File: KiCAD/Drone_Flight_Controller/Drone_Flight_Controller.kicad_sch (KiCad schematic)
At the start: 0 parts

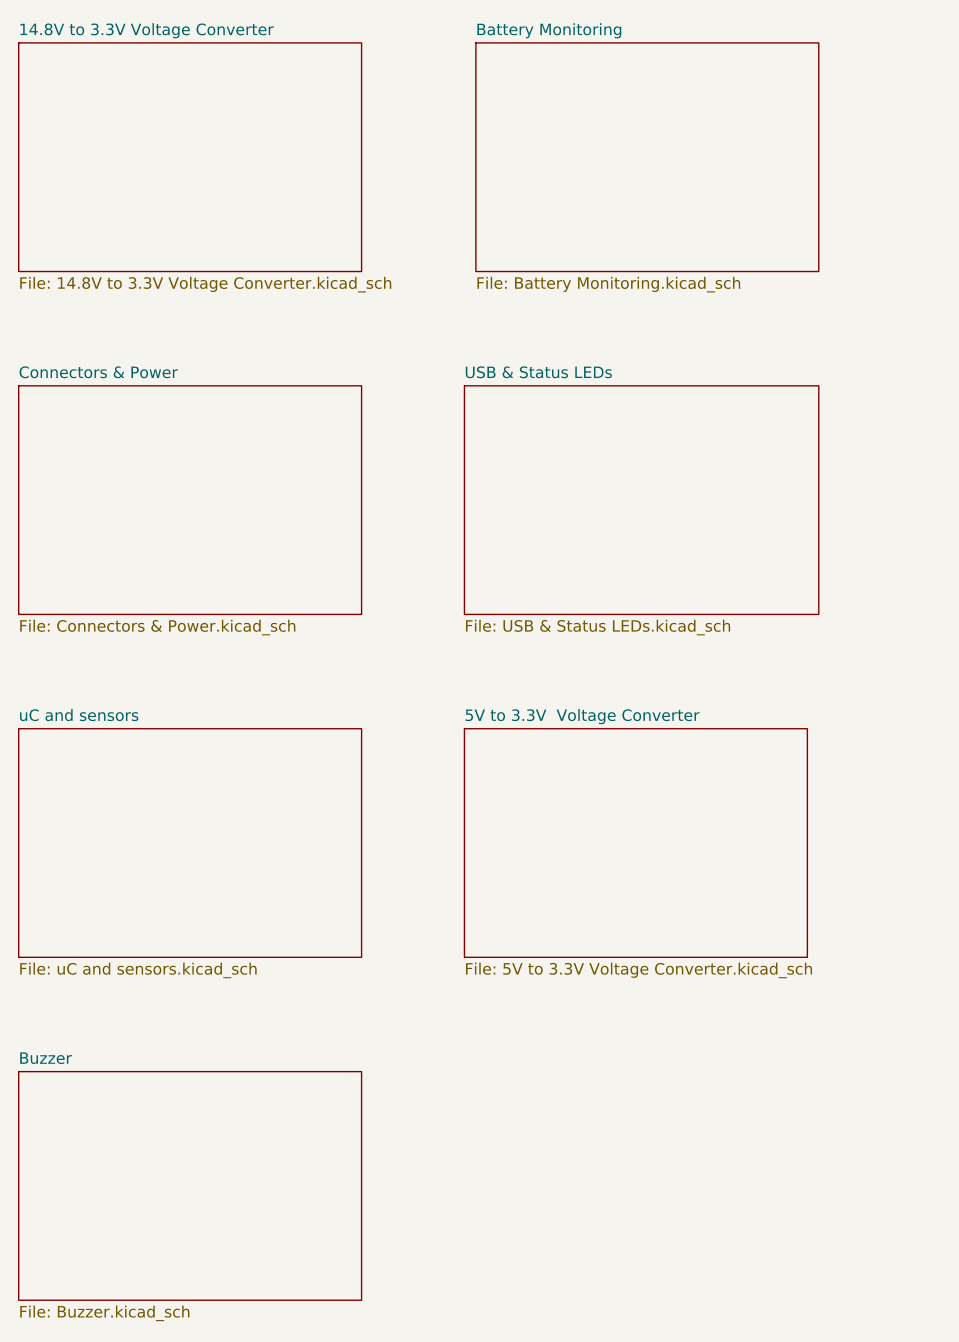
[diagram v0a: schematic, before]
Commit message: Remove 14.8V to 3.3V Voltage Converter
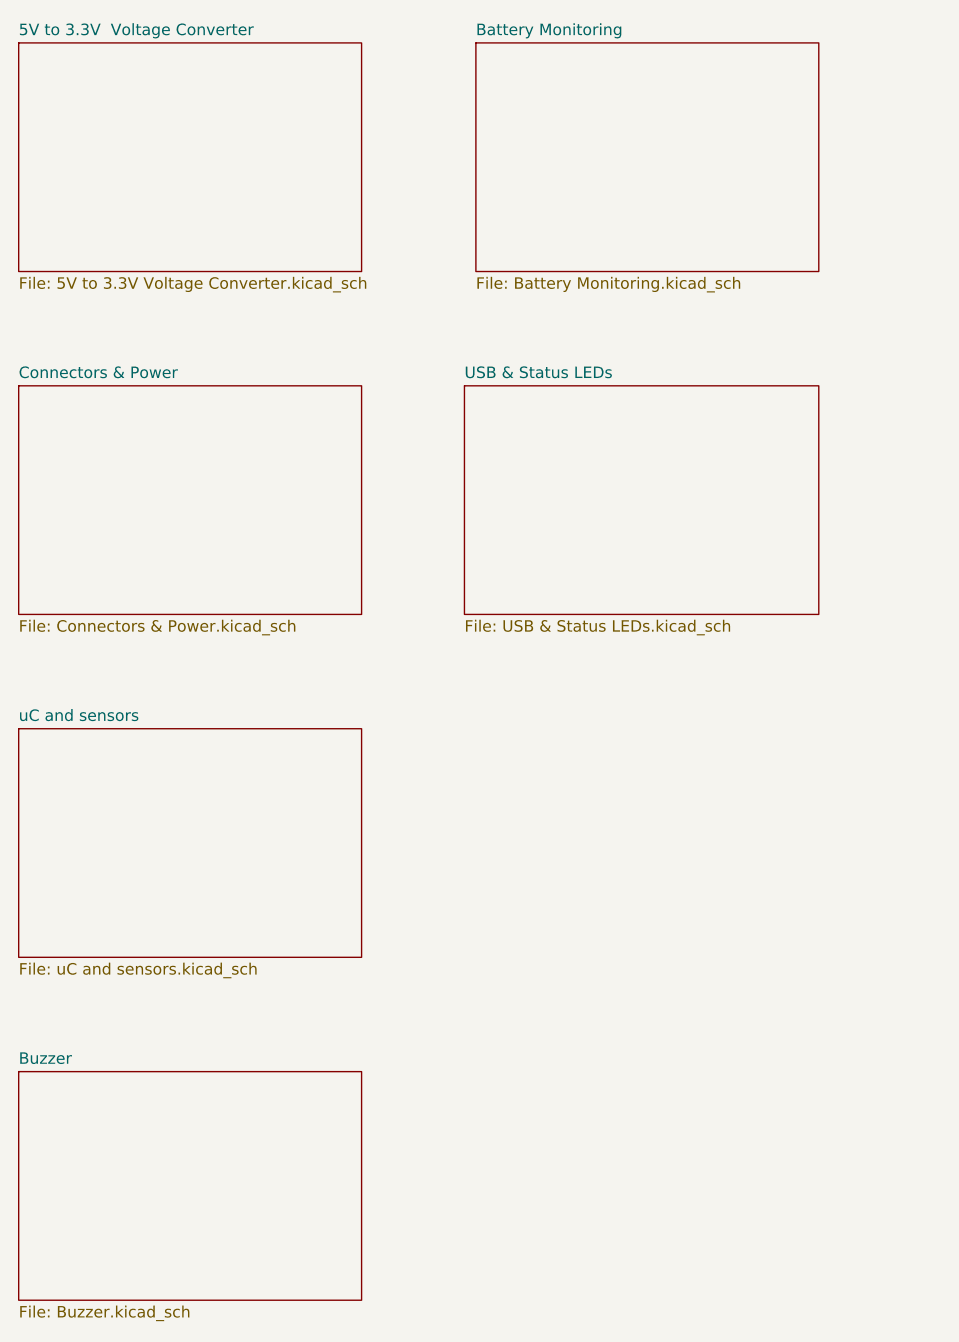
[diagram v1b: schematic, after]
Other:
- removed sheet 14.8V to 3.3V Voltage Converter
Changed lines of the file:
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@@
 	(title_block
 		(title "Drone Flight Controller")
-		(date "2025-07-07")
-		(rev "V1")
+		(date "2025-09-19")
+		(rev "V2")
 		(company "HTL Steyr")
 		(comment 1 "Brandner; Hinterberger")
@@
 	)
 	(sheet
-		(at 74.93 101.6)
+		(at 25.4 25.4)
 		(size 38.1 25.4)
 		(exclude_from_sim no)
@@
 		)
 		(property "Sheetname" "5V to 3.3V  Voltage Converter"
-			(at 74.93 100.8884 0)
+			(at 25.4 24.6884 0)
 			(effects
 				(font
@@
 		)
 		(property "Sheetfile" "5V to 3.3V Voltage Converter.kicad_sch"
-			(at 74.93 127.5846 0)
+			(at 25.4 51.3846 0)
 			(effects
 				(font
@@
 				)
 			)
-		)
-	)
-	(sheet
-		(at 25.4 25.4)
-		(size 38.1 25.4)
-		(exclude_from_sim no)
-		(in_bom yes)
-		(on_board yes)
-		(dnp no)
-		(fields_autoplaced yes)
-		(stroke
-			(width 0.1524)
-			(type solid)
-		)
-		(fill
-			(color 0 0 0 0.0000)
-		)
-		(property "Sheetname" "14.8V to 3.3V Voltage Converter"
-			(at 25.4 24.6884 0)
-			(effects
-				(font
-					(size 1.27 1.27)
-				)
-				(justify left bottom)
-			)
-		)
-		(property "Sheetfile" "14.8V to 3.3V Voltage Converter.kicad_sch"
-			(at 25.4 51.3846 0)
-			(effects
-				(font
-					(size 1.27 1.27)
-				)
-				(justify left top)
-			)
-		)
-		(instances
-			(project "Drone_Flight_Controller"
-				(path "/05daaa24-e506-4b9a-9564-8bf799413ca8"
-					(page "2")
-				)
-			)
